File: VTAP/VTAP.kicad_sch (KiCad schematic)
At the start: 40 parts, among them J1 MX 52901-0274

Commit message: VTAP update
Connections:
- net GND: now also F0.2; no longer F0.1
- net TP1: now also F1.1; no longer F1.2
- net TP10: now also F10.2; no longer F10.1
- net TP11: now also F11.1; no longer F11.2
- net TP12: now also F12.2; no longer F12.1
- net TP13: now also F13.1; no longer F13.2
- net TP14: now also F14.2; no longer F14.1
- net TP2: now also F2.2; no longer F2.1
- net TP3: now also F3.1; no longer F3.2
- net TP4: now also F4.2; no longer F4.1
- net TP5: now also F5.1; no longer F5.2
- net TP6: now also F6.2; no longer F6.1
- net TP7: now also F7.1; no longer F7.2
- net TP8: now also F8.2; no longer F8.1
- net TP9: now also F9.1; no longer F9.2
- net at TP12.1: now also F12.1; no longer F12.2
- net at TP1.1: now also F1.2; no longer F1.1
- net at TP13.1: now also F13.2; no longer F13.1
- net at TP11.1: now also F11.2; no longer F11.1
- net at TP6.1: now also F6.1; no longer F6.2
- net at TP5.1: now also F5.2; no longer F5.1
- net at TP7.1: now also F7.2; no longer F7.1
- net at TP4.1: now also F4.1; no longer F4.2
- net at TP8.1: now also F8.1; no longer F8.2
- net at TP14.1: now also F14.1; no longer F14.2
- net at TP10.1: now also F10.1; no longer F10.2
- net at TP2.1: now also F2.1; no longer F2.2
- net at TP3.1: now also F3.2; no longer F3.1
- net at TP0.1: now also F0.1; no longer F0.2
- net at TP9.1: now also F9.2; no longer F9.1
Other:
- moved on the sheet: F0, F1, F10, F11, F12, F13, F14, F2, F3, F4, F5, F6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
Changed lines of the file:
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@@
 	(symbol
 		(lib_id "Device:Fuse")
-		(at 219.71 111.76 90)
+		(at 219.71 111.76 270)
+		(mirror x)
 		(unit 1)
 		(exclude_from_sim no)
@@
 	(symbol
 		(lib_id "Device:Fuse")
-		(at 219.71 81.28 90)
+		(at 219.71 81.28 270)
+		(mirror x)
 		(unit 1)
 		(exclude_from_sim no)
@@
 	(symbol
 		(lib_id "Device:Fuse")
-		(at 219.71 86.36 90)
+		(at 219.71 86.36 270)
+		(mirror x)
 		(unit 1)
 		(exclude_from_sim no)
@@
 	(symbol
 		(lib_id "Device:Fuse")
-		(at 199.39 83.82 90)
+		(at 199.39 83.82 270)
+		(mirror x)
 		(unit 1)
 		(exclude_from_sim no)
@@
 	(symbol
 		(lib_id "Device:Fuse")
-		(at 219.71 96.52 90)
+		(at 219.71 96.52 270)
+		(mirror x)
 		(unit 1)
 		(exclude_from_sim no)
@@
 	(symbol
 		(lib_id "Device:Fuse")
-		(at 199.39 93.98 90)
+		(at 199.39 93.98 270)
+		(mirror x)
 		(unit 1)
 		(exclude_from_sim no)
@@
 	(symbol
 		(lib_id "Device:Fuse")
-		(at 199.39 104.14 90)
+		(at 199.39 104.14 270)
+		(mirror x)
 		(unit 1)
 		(exclude_from_sim no)
@@
 	(symbol
 		(lib_id "Device:Fuse")
-		(at 199.39 88.9 90)
+		(at 199.39 88.9 270)
+		(mirror x)
 		(unit 1)
 		(exclude_from_sim no)
@@
 	(symbol
 		(lib_id "Device:Fuse")
-		(at 199.39 109.22 90)
+		(at 199.39 109.22 270)
+		(mirror x)
 		(unit 1)
 		(exclude_from_sim no)
@@
 	(symbol
 		(lib_id "Device:Fuse")
-		(at 219.71 106.68 90)
+		(at 219.71 106.68 270)
+		(mirror x)
 		(unit 1)
 		(exclude_from_sim no)
@@
 	(symbol
 		(lib_id "Device:Fuse")
-		(at 219.71 91.44 90)
+		(at 219.71 91.44 270)
+		(mirror x)
 		(unit 1)
 		(exclude_from_sim no)
@@
 	(symbol
 		(lib_id "Device:Fuse")
-		(at 219.71 101.6 90)
+		(at 219.71 101.6 270)
+		(mirror x)
 		(unit 1)
 		(exclude_from_sim no)
@@
 	(symbol
 		(lib_id "Device:Fuse")
-		(at 199.39 114.3 90)
+		(at 199.39 114.3 270)
+		(mirror x)
 		(unit 1)
 		(exclude_from_sim no)
@@
 	(symbol
 		(lib_id "Device:Fuse")
-		(at 199.39 99.06 90)
+		(at 199.39 99.06 270)
+		(mirror x)
 		(unit 1)
 		(exclude_from_sim no)
@@
 	(symbol
 		(lib_id "Device:Fuse")
-		(at 199.39 78.74 90)
-		(unit 1)
-		(exclude_from_sim no)
+		(at 199.39 78.74 270)
+		(mirror x)
+		(unit 1)
+		(exclude_from_sim no)

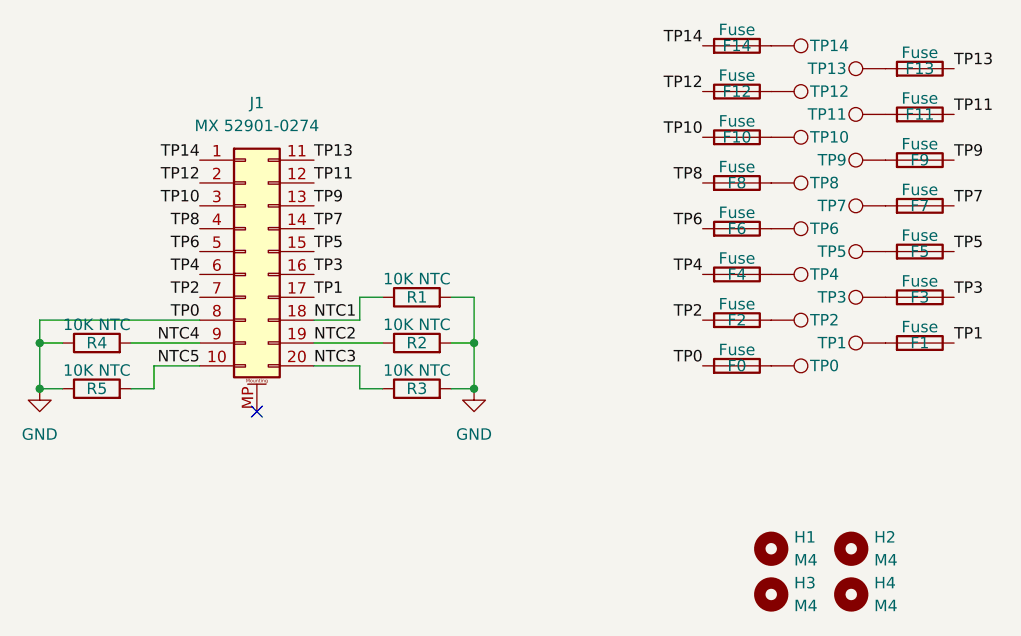
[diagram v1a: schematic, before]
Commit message: VTAP with new spacing
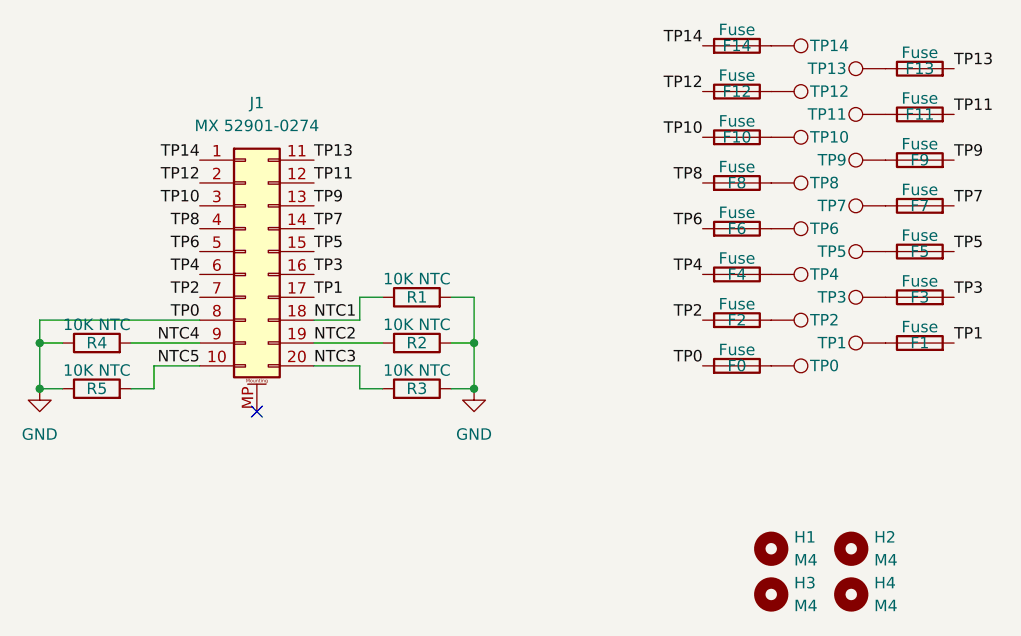
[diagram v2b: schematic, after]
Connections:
- net GND: now also R2.1, R3.1; no longer R2.2, R3.2
- net NTC2: now also R2.2; no longer R2.1
- net NTC3: now also R3.2; no longer R3.1
- net TP1: now also F1.2; no longer F1.1
- net TP11: now also F11.2; no longer F11.1
- net TP13: now also F13.2; no longer F13.1
- net TP3: now also F3.2; no longer F3.1
- net TP5: now also F5.2; no longer F5.1
- net TP7: now also F7.2; no longer F7.1
- net TP9: now also F9.2; no longer F9.1
- net at TP1.1: now also F1.1; no longer F1.2
- net at TP13.1: now also F13.1; no longer F13.2
- net at TP11.1: now also F11.1; no longer F11.2
- net at TP5.1: now also F5.1; no longer F5.2
- net at TP7.1: now also F7.1; no longer F7.2
- net at TP3.1: now also F3.1; no longer F3.2
- net at TP9.1: now also F9.1; no longer F9.2
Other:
- moved on the sheet: F1, F11, F13, F3, F5, F7, F9, R2, R3
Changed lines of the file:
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@@
 	(symbol
 		(lib_id "Device:Fuse")
-		(at 219.71 111.76 270)
-		(mirror x)
+		(at 219.71 111.76 90)
 		(unit 1)
 		(exclude_from_sim no)
@@
 	(symbol
 		(lib_id "Device:Fuse")
-		(at 219.71 81.28 270)
-		(mirror x)
+		(at 219.71 81.28 90)
 		(unit 1)
 		(exclude_from_sim no)
@@
 	(symbol
 		(lib_id "Device:Fuse")
-		(at 219.71 86.36 270)
-		(mirror x)
+		(at 219.71 86.36 90)
 		(unit 1)
 		(exclude_from_sim no)
@@
 	(symbol
 		(lib_id "Device:Fuse")
-		(at 219.71 96.52 270)
-		(mirror x)
+		(at 219.71 96.52 90)
 		(unit 1)
 		(exclude_from_sim no)
@@
 	(symbol
 		(lib_id "Device:R")
-		(at 163.83 116.84 90)
+		(at 163.83 116.84 270)
+		(mirror x)
 		(unit 1)
 		(exclude_from_sim no)
@@
 	(symbol
 		(lib_id "Device:R")
-		(at 163.83 111.76 90)
+		(at 163.83 111.76 270)
+		(mirror x)
 		(unit 1)
 		(exclude_from_sim no)
@@
 	(symbol
 		(lib_id "Device:Fuse")
-		(at 219.71 106.68 270)
-		(mirror x)
+		(at 219.71 106.68 90)
 		(unit 1)
 		(exclude_from_sim no)
@@
 	(symbol
 		(lib_id "Device:Fuse")
-		(at 219.71 91.44 270)
-		(mirror x)
+		(at 219.71 91.44 90)
 		(unit 1)
 		(exclude_from_sim no)
@@
 	(symbol
 		(lib_id "Device:Fuse")
-		(at 219.71 101.6 270)
-		(mirror x)
-		(unit 1)
-		(exclude_from_sim no)
+		(at 219.71 101.6 90)
+		(unit 1)
+		(exclude_from_sim no)
